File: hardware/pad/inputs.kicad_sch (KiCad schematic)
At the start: 28 parts, among them J5 Selector ON-OFF-ON, SW1 Razer Yellow (MX, hot-swap), SW10 Razer Yellow (MX, hot-swap), SW11 Razer Yellow (MX, hot-swap), SW12 Razer Yellow (MX, hot-swap), SW13 PEC11R-4220F-S0024, SW14 PEC11R-4220F-S0024, SW2 Razer Yellow (MX, hot-swap), SW3 Razer Yellow (MX, hot-swap), SW4 Razer Yellow (MX, hot-swap), SW5 Razer Yellow (MX, hot-swap), SW6 Razer Yellow (MX, hot-swap), SW7 Razer Yellow (MX, hot-swap), SW8 Razer Yellow (MX, hot-swap), SW9 Razer Yellow (MX, hot-swap), U6 TCA9555PWR

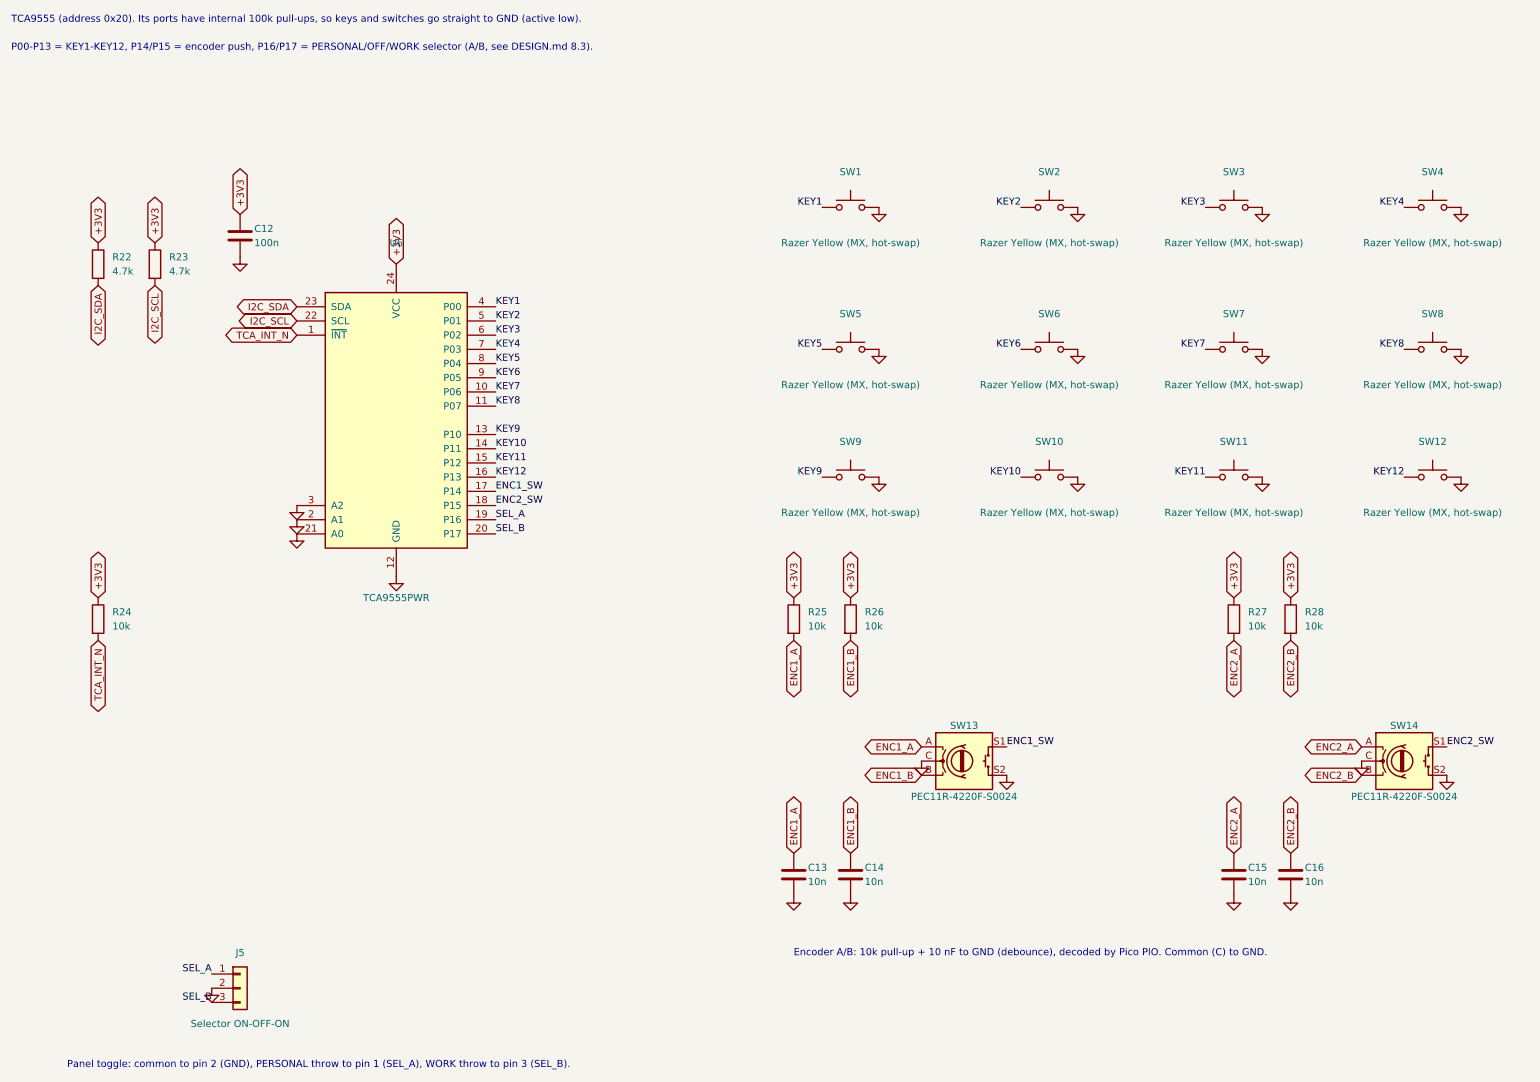
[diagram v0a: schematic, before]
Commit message: Pad schematic: hand-redrawn from the connection guide; netlist verified against the reference
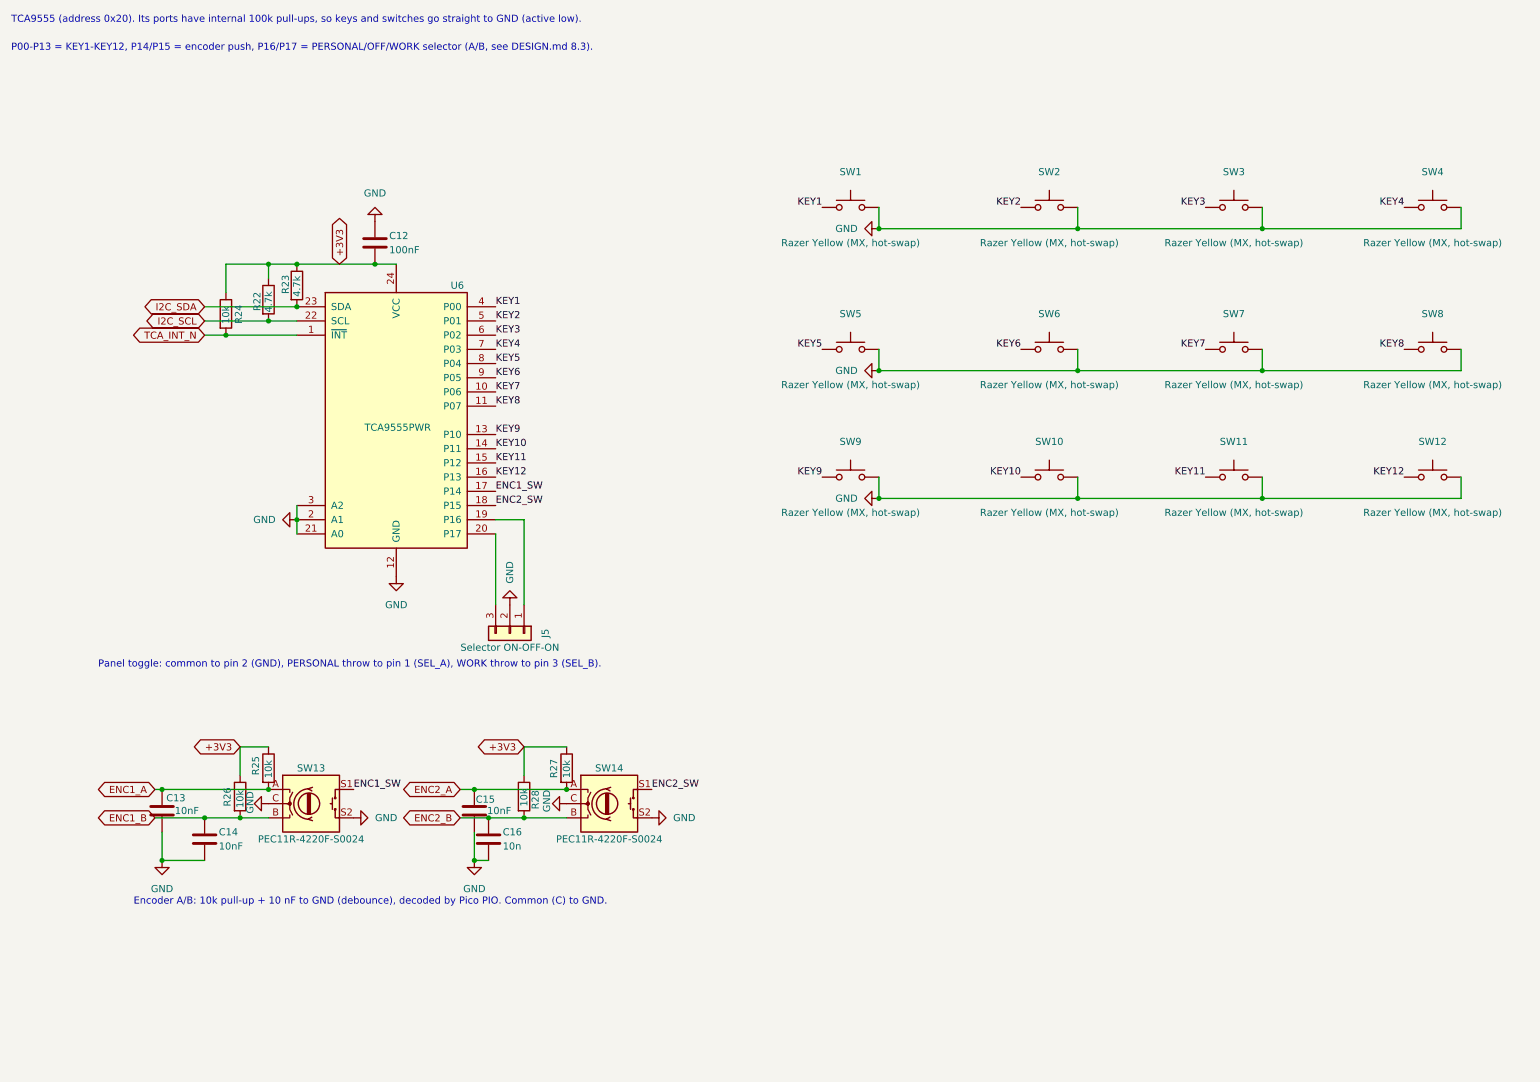
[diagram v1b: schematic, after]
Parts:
- C12: value 100n -> 100nF
- C13, C14, C15: value 10n -> 10nF
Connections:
- net +3V3: now also C12.2; no longer C12.1
- net GND: now also C12.1; no longer C12.2
- net I2C_SCL: now also R22.2; no longer R23.2
- net I2C_SDA: now also R23.2; no longer R22.2
- net SEL_A: no longer names the net of J5.1 (Pin_1), U6.19 (P16)
- net SEL_B: no longer names the net of J5.3 (Pin_3), U6.20 (P17)
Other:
- moved on the sheet: J5, SW13, SW14
